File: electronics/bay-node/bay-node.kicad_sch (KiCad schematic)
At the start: 0 parts

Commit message: DATA lead on 8 wires: node J7 a vertical PH 8 (USB, I²C, INT), data port J2 an S8B
Density decisions of 2026-10-19: the DATA lead becomes the camera's PH 8
"Same direction" type and also carries the node's I²C and an open-drain,
active-low INT (IO4, 10k pull-up, 1k at J7) for a later DATA ×4 board.

- Node: J7 B8B vertical by the right edge (J5's old slot), J5 AUX
  horizontal in the middle, AUX parts in a column between them.  J7 now
  taps the pair at J4's pads (DUT_CONN_*, behind U8's ESD like J4); the
  branch is hand-drawn in usb_hs_routes() on B.Cu under J4, since
  Freerouting found no room on U8's mux side.  ERC 0, DRC 0, parity 0,
  99 models.
- Data port: S8B, pins 1–3 open, PH at x 14.4, left hole (2.6, 13.5),
  one silkscreen label per pin.  ERC 0, DRC 0, parity 0.
- Pin map (README, check_pinmap: DATA_INT reserved), docs, cabling,
  BOM (one PH 8 lead type for DATA and camera, no B5B/S5B), SCAD config.

Co-Authored-By: Claude Opus 5.5 <noreply@anthropic.com>
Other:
- note added: "DATA_INT, ESP_DN/DP, I2C_SCL/SDA,"
- note added: "DUT_5V, I2C_SCL/SDA"
- note added: "MUX_FORCE_PC, PC_DET, SVC"
- note removed: "DUT_5V"
- note removed: "ESP_DN/DP, MUX_FORCE_PC, PC_DET, SVC"
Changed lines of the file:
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@@
 		(pts
 			(xy 91.44 100.33)
-			(xy 91.44 110.49)
-			(xy 138.43 110.49)
+			(xy 91.44 113.03)
+			(xy 138.43 113.03)
 			(xy 138.43 100.33)
 		)
@@
 		)
 	)
-	(text "ESP_DN/DP, MUX_FORCE_PC, PC_DET, SVC"
+	(text "DATA_INT, ESP_DN/DP, I2C_SCL/SDA,"
 		(exclude_from_sim no)
 		(at 93.98 109.22 0)
+		(effects
+			(font
+				(size 1.4 1.4)
+			)
+			(justify left bottom)
+		)
+	)
+	(text "MUX_FORCE_PC, PC_DET, SVC"
+		(exclude_from_sim no)
+		(at 93.98 111.76 0)
 		(effects
 			(font
@@
 		(pts
 			(xy 179.07 100.33)
-			(xy 179.07 120.65)
-			(xy 232.41 120.65)
+			(xy 179.07 123.19)
+			(xy 232.41 123.19)
 			(xy 232.41 100.33)
 		)
@@
 		)
 	)
-	(text "DUT_5V"
+	(text "DUT_5V, I2C_SCL/SDA"
 		(exclude_from_sim no)
-		(at 181.61 119.38 0)
+		(at 181.61 121.92 0)
 		(effects
 			(font
@@
 		(pts
 			(xy 83.82 100.33)
-			(xy 83.82 130.81)
-			(xy 240.03 130.81)
+			(xy 83.82 133.35)
+			(xy 240.03 133.35)
 			(xy 240.03 100.33)
 		)
@@
 	(text "AUX_BOOT_CTL, AUX_RST_CTL, AUX_RX/TX, DUT_EN, DUT_FLT_N, I2C_SCL/SDA, INA_ALERT_N"
 		(exclude_from_sim no)
-		(at 86.36 129.54 0)
+		(at 86.36 132.08 0)
 		(effects
 			(font
@@
 		(pts
 			(xy 76.2 100.33)
-			(xy 76.2 140.97)
-			(xy 327.66 140.97)
+			(xy 76.2 143.51)
+			(xy 327.66 143.51)
 			(xy 327.66 100.33)
 		)
@@
 	(text "CAN_RXD/TXD, POS_IN/OUT"
 		(exclude_from_sim no)
-		(at 78.74 139.7 0)
+		(at 78.74 142.24 0)
 		(effects
 			(font
@@
 		(pts
 			(xy -2.54 100.33)
-			(xy -2.54 151.13)
-			(xy 335.28 151.13)
+			(xy -2.54 153.67)
+			(xy 335.28 153.67)
 			(xy 335.28 100.33)
 		)
@@
 	(text "CAN_H/L, POS_IN_CONN, POS_OUT_CONN"
 		(exclude_from_sim no)
-		(at 0 149.86 0)
+		(at 0 152.4 0)
 		(effects
 			(font
@@
 		(pts
 			(xy 68.58 100.33)
-			(xy 68.58 161.29)
-			(xy 421.64 161.29)
+			(xy 68.58 163.83)
+			(xy 421.64 163.83)
 			(xy 421.64 100.33)
 		)
@@
 	(text "CAM_CS/LED/SCK, CAM_MISO, CAM_MOSI"
 		(exclude_from_sim no)
-		(at 71.12 160.02 0)
+		(at 71.12 162.56 0)
 		(effects
 			(font
@@
 	(text_box "Bay node — one per bay.  Sheets:\n  Power: row cable (JST PH 6: bus, GND, CAN_H, CAN_L, GND, POS), reverse protection, LMR51635 buck, AMS1117\n  MCU: ESP32-S3-WROOM-1-N8R8 (8 MB flash, 8 MB octal PSRAM), reset/boot, status LED, UART pads\n  USB: front PC port, DUT port, two FSUSB42 muxes + OR gate (classic / USB-IP / service modes)\n  DUT power & AUX: TPS2553 switch → shunt → DUT_5V, INA226 monitor, AUX UART/RESET/BOOT\n  Camera: JST PH 8 to the bay's Arducam Mega (SPI2, 5 V through a PTC) and its LEDs (AO3400A low side)\n  Rack bus: TCAN1462V CAN transceiver on the row pair, POS token in/out (docs/can.md)\n\nMode truth table:  SERVICE=0, PC unplugged → DUT↔ESP32 (USB/IP)\n                   SERVICE=0, PC plugged   → DUT↔PC (classic), ESP32 still controls DUT_5V/AUX\n                   SERVICE=1               → PC↔ESP32 (flash/console), DUT data disconnected\nGPIO firmware can also force classic mode (MUX_FORCE_PC)."
 		(exclude_from_sim no)
-		(at 30 176.53 0)
+		(at 30 179.07 0)
 		(size 360 33.02)
 		(margins 2 2 2 2)

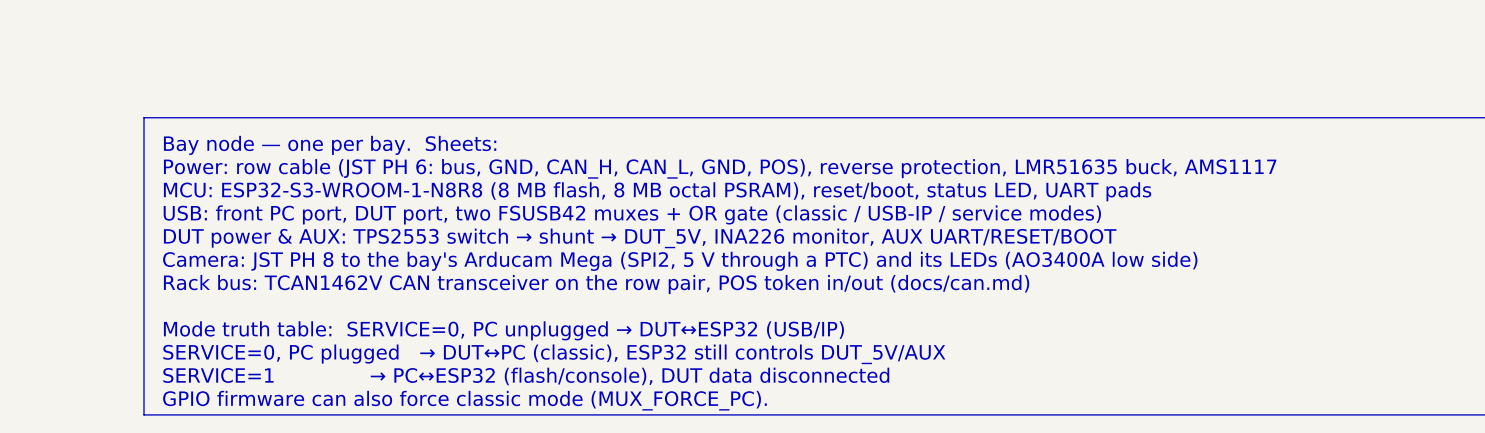
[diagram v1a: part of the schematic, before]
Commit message: CAN transceiver: the TJA1462AT on the hub and the node
The TCAN1462V (C7399456) had no LCSC stock on 2026-10-18 and 19, and
JLC's quote of the hub asked for another part.  The user chose NXP's
TJA1462AT/0Z (C3234095, 10 500 in stock) for both boards (hub U6, node
U11): the same SOIC-8 pinout (VIO on pin 5, STB on pin 8), signal
improvement kept, bus pins -36/+40 V instead of ±58 V.  The TCAN1462V
and the TCAN1044AV stay the alternates.

Both boards regenerated and the same Freerouting sessions re-imported
(tracks and vias unchanged): ERC 0, DRC 0 errors (the hub's known C8
silkscreen warning), 0 unconnected, parity 0, JLC READY.  The CPL keeps
its 270° correction (C3234095 was already in build_board.py).

Docs: can.md, electronics.md, firmware comments and pin tables,
bom/sourcing.md, which also notes that JLC unticks the USB4105 (hard to
process, $0.03 a piece): tick it again at every order.

Co-Authored-By: Claude Opus 5.5 <noreply@anthropic.com>
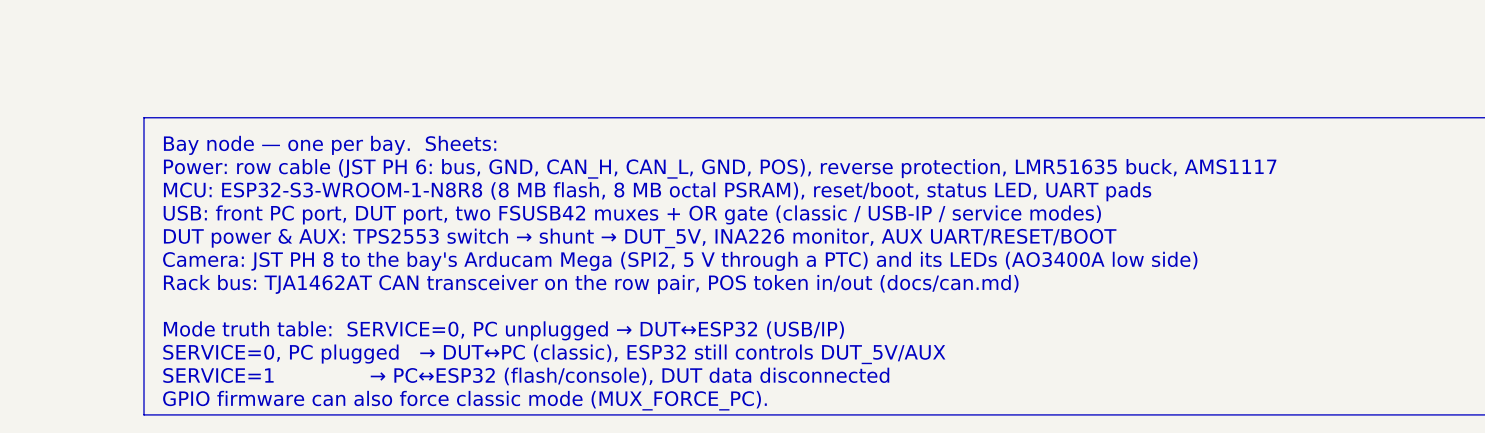
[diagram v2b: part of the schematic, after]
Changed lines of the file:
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@@
 		)
 	)
-	(text_box "Bay node — one per bay.  Sheets:\n  Power: row cable (JST PH 6: bus, GND, CAN_H, CAN_L, GND, POS), reverse protection, LMR51635 buck, AMS1117\n  MCU: ESP32-S3-WROOM-1-N8R8 (8 MB flash, 8 MB octal PSRAM), reset/boot, status LED, UART pads\n  USB: front PC port, DUT port, two FSUSB42 muxes + OR gate (classic / USB-IP / service modes)\n  DUT power & AUX: TPS2553 switch → shunt → DUT_5V, INA226 monitor, AUX UART/RESET/BOOT\n  Camera: JST PH 8 to the bay's Arducam Mega (SPI2, 5 V through a PTC) and its LEDs (AO3400A low side)\n  Rack bus: TCAN1462V CAN transceiver on the row pair, POS token in/out (docs/can.md)\n\nMode truth table:  SERVICE=0, PC unplugged → DUT↔ESP32 (USB/IP)\n                   SERVICE=0, PC plugged   → DUT↔PC (classic), ESP32 still controls DUT_5V/AUX\n                   SERVICE=1               → PC↔ESP32 (flash/console), DUT data disconnected\nGPIO firmware can also force classic mode (MUX_FORCE_PC)."
+	(text_box "Bay node — one per bay.  Sheets:\n  Power: row cable (JST PH 6: bus, GND, CAN_H, CAN_L, GND, POS), reverse protection, LMR51635 buck, AMS1117\n  MCU: ESP32-S3-WROOM-1-N8R8 (8 MB flash, 8 MB octal PSRAM), reset/boot, status LED, UART pads\n  USB: front PC port, DUT port, two FSUSB42 muxes + OR gate (classic / USB-IP / service modes)\n  DUT power & AUX: TPS2553 switch → shunt → DUT_5V, INA226 monitor, AUX UART/RESET/BOOT\n  Camera: JST PH 8 to the bay's Arducam Mega (SPI2, 5 V through a PTC) and its LEDs (AO3400A low side)\n  Rack bus: TJA1462AT CAN transceiver on the row pair, POS token in/out (docs/can.md)\n\nMode truth table:  SERVICE=0, PC unplugged → DUT↔ESP32 (USB/IP)\n                   SERVICE=0, PC plugged   → DUT↔PC (classic), ESP32 still controls DUT_5V/AUX\n                   SERVICE=1               → PC↔ESP32 (flash/console), DUT data disconnected\nGPIO firmware can also force classic mode (MUX_FORCE_PC)."
 		(exclude_from_sim no)
 		(at 30 179.07 0)

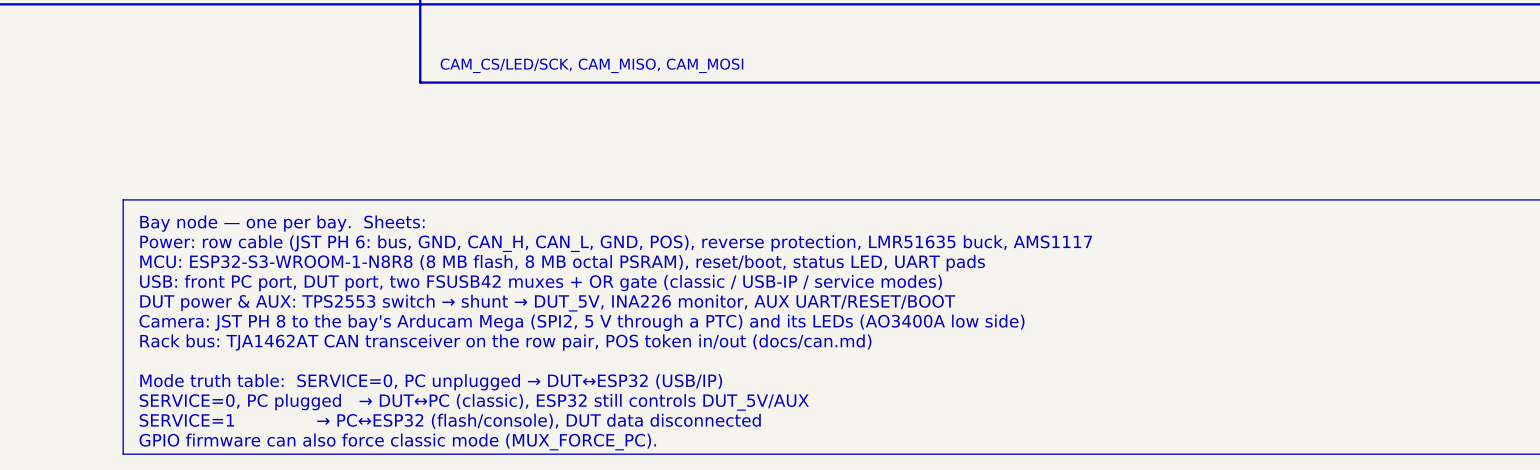
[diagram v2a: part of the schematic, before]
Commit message: Node 5 V buck: LMR51625 with TI's 4.7 µH
The bay node's U1 goes from the LMR51635YDDCR (3.5 A) to its 2.5 A
sibling, the LMR51625YDDCR (C44991044), as the user asked.  TI SLUSF64B
covers both parts: they have the same DDC package and pinout (FB 1,
EN 2, VIN 3, GND 4, SW 5, CB 6), the same 0.8 V reference, the same EN
thresholds and the same 63 V absolute maximum.

L1 goes to 4.7 µH, per SLUSF64B table 8-1 (LMR51625, 5 V, 1.1 MHz).
The new part is the FXL0630-4R7-M (C167220), in the same footprint:
9 A saturation, 6 A rms, 33 mΩ.  The existing 3 × 22 µF output meets
the table's 22 µF.

Current headroom: a bay draws at most 2.2 A (node 0.30 A, the DUT
switch's 1.52 A, camera 0.36 A).  From 28 V the inductor then peaks at
about 2.6 A (0.8 A ripple), under the 2.5 A part's 2.9 A minimum peak
limit.  With 3.3 µH the peak would be 2.74 A.

The hub keeps the LMR51635 under the "buck" catalogue key.  The node
uses two new keys, "buck25" and "buck_l47".

CPL: JLC's EasyEDA footprint of C44991044 is pad for pad that of
C45262770 and C7519, so it gets the same 270° correction.  C167220
shares C167219's footprint and needs no correction.

Board: schematic regenerated; the routed PCB keeps its routing (only
U1 and L1 properties change, copied from a fresh build).  ERC 0,
DRC 0, unconnected 0, parity 0.  Gerbers, CPL and renders unchanged.

Cost:
- node order $322.96 -> $316.95 (-$6.01 components: LCSC $1.0744
  against $1.5997 at 10, the inductor $0.096 against $0.107, × 1.12);
- one rack's JLC boards $752.95 -> $746.43 (5 racks $310.59,
  10 racks $257.85);
- BOM total €1,013 -> €1,007 (€126 a bay);
- the 9-instead-of-10 lever is now $2.34.

The parts snapshot gains the two parts.  The BOM note prints a
negative adjustment as "− $6.01", not "+ $-6.01".

Co-Authored-By: Claude Opus 5.5 <noreply@anthropic.com>
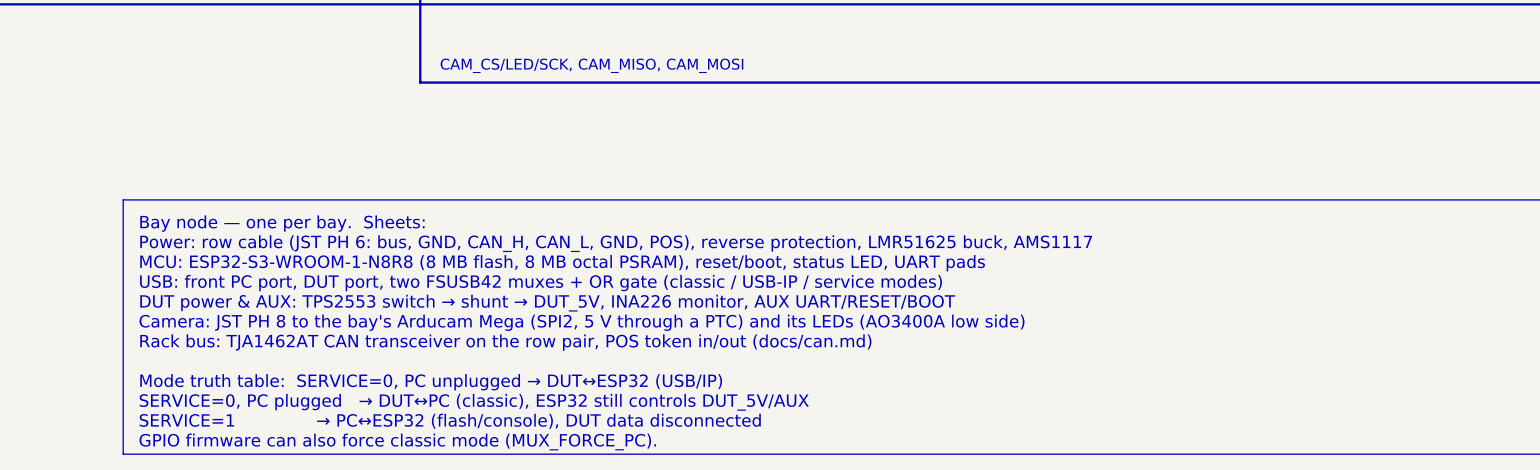
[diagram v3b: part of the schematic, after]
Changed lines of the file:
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@@
 		)
 	)
-	(text_box "Bay node — one per bay.  Sheets:\n  Power: row cable (JST PH 6: bus, GND, CAN_H, CAN_L, GND, POS), reverse protection, LMR51635 buck, AMS1117\n  MCU: ESP32-S3-WROOM-1-N8R8 (8 MB flash, 8 MB octal PSRAM), reset/boot, status LED, UART pads\n  USB: front PC port, DUT port, two FSUSB42 muxes + OR gate (classic / USB-IP / service modes)\n  DUT power & AUX: TPS2553 switch → shunt → DUT_5V, INA226 monitor, AUX UART/RESET/BOOT\n  Camera: JST PH 8 to the bay's Arducam Mega (SPI2, 5 V through a PTC) and its LEDs (AO3400A low side)\n  Rack bus: TJA1462AT CAN transceiver on the row pair, POS token in/out (docs/can.md)\n\nMode truth table:  SERVICE=0, PC unplugged → DUT↔ESP32 (USB/IP)\n                   SERVICE=0, PC plugged   → DUT↔PC (classic), ESP32 still controls DUT_5V/AUX\n                   SERVICE=1               → PC↔ESP32 (flash/console), DUT data disconnected\nGPIO firmware can also force classic mode (MUX_FORCE_PC)."
+	(text_box "Bay node — one per bay.  Sheets:\n  Power: row cable (JST PH 6: bus, GND, CAN_H, CAN_L, GND, POS), reverse protection, LMR51625 buck, AMS1117\n  MCU: ESP32-S3-WROOM-1-N8R8 (8 MB flash, 8 MB octal PSRAM), reset/boot, status LED, UART pads\n  USB: front PC port, DUT port, two FSUSB42 muxes + OR gate (classic / USB-IP / service modes)\n  DUT power & AUX: TPS2553 switch → shunt → DUT_5V, INA226 monitor, AUX UART/RESET/BOOT\n  Camera: JST PH 8 to the bay's Arducam Mega (SPI2, 5 V through a PTC) and its LEDs (AO3400A low side)\n  Rack bus: TJA1462AT CAN transceiver on the row pair, POS token in/out (docs/can.md)\n\nMode truth table:  SERVICE=0, PC unplugged → DUT↔ESP32 (USB/IP)\n                   SERVICE=0, PC plugged   → DUT↔PC (classic), ESP32 still controls DUT_5V/AUX\n                   SERVICE=1               → PC↔ESP32 (flash/console), DUT data disconnected\nGPIO firmware can also force classic mode (MUX_FORCE_PC)."
 		(exclude_from_sim no)
 		(at 30 179.07 0)

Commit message: Bay node: AP2114H for the 3.3 V, camera ESD clamped to +3V3
The schematic counter-review's fixes, approved by the user.

- U2: AP2114H-3.3TRG1 (C150716, catalog ldo_1a) instead of the AMS1117-3.3.
  It is specified stable with ceramics (C11, C12); the AMS1117 guarantees it
  only with 22 uF tantalum.  Same SOT-223 "H" pinout (1 GND, 2 and tab VOUT,
  3 VIN), footprint and copper: only the part's properties change.
- U12, U13 (USBLC6 on the camera lead): pin 5 on +3V3 instead of CAM_5V.
  With CAM_5V off (the PTC tripped), the SPI lines would feed the pod through
  the upper diodes, and CAM_5V's clamp sits above the ESP32's 3.6 V.  A
  minimal patch of the routing, no re-route: the CAM_5V stub that only
  reached the two pins goes (10 segments); U12.5 gets a +3V3 feed to a via in
  In2's +3V3 area; U13.5, with no room for its own, joins U12.5 along the
  stub's old east path at 0.25 mm.  The straightening pass ran on +3V3 and
  CAM_5V.
- Stale notes: AUX_VREF goes through R23's 1k, not 33 ohms; the next node's
  pull-down is R29's 470k, not 100k.
- pcbgen.fanout_pads takes `only` (REF.PAD), to fan out a few pads of a
  routed board.

ERC 0, DRC 0, unconnected 0, parity 0, every 3D model found.  The renders,
Gerbers and viewer model are regenerated (the unchanged iso render kept).
The schematic, the BOM and the docs (the node table, the CPL fix table, the
bring-up check, PCBA review N9) follow.  The hub and bom/ are untouched.

Co-Authored-By: Claude Opus 5.5 <noreply@anthropic.com>
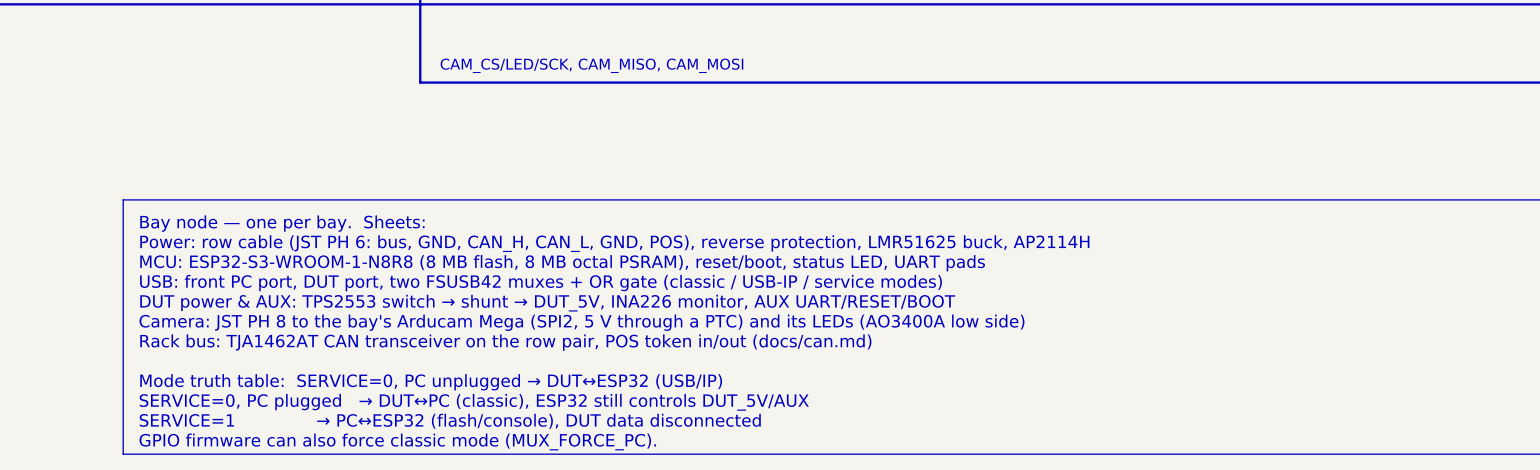
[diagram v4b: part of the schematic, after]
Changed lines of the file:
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@@
 		)
 	)
-	(text_box "Bay node — one per bay.  Sheets:\n  Power: row cable (JST PH 6: bus, GND, CAN_H, CAN_L, GND, POS), reverse protection, LMR51625 buck, AMS1117\n  MCU: ESP32-S3-WROOM-1-N8R8 (8 MB flash, 8 MB octal PSRAM), reset/boot, status LED, UART pads\n  USB: front PC port, DUT port, two FSUSB42 muxes + OR gate (classic / USB-IP / service modes)\n  DUT power & AUX: TPS2553 switch → shunt → DUT_5V, INA226 monitor, AUX UART/RESET/BOOT\n  Camera: JST PH 8 to the bay's Arducam Mega (SPI2, 5 V through a PTC) and its LEDs (AO3400A low side)\n  Rack bus: TJA1462AT CAN transceiver on the row pair, POS token in/out (docs/can.md)\n\nMode truth table:  SERVICE=0, PC unplugged → DUT↔ESP32 (USB/IP)\n                   SERVICE=0, PC plugged   → DUT↔PC (classic), ESP32 still controls DUT_5V/AUX\n                   SERVICE=1               → PC↔ESP32 (flash/console), DUT data disconnected\nGPIO firmware can also force classic mode (MUX_FORCE_PC)."
+	(text_box "Bay node — one per bay.  Sheets:\n  Power: row cable (JST PH 6: bus, GND, CAN_H, CAN_L, GND, POS), reverse protection, LMR51625 buck, AP2114H\n  MCU: ESP32-S3-WROOM-1-N8R8 (8 MB flash, 8 MB octal PSRAM), reset/boot, status LED, UART pads\n  USB: front PC port, DUT port, two FSUSB42 muxes + OR gate (classic / USB-IP / service modes)\n  DUT power & AUX: TPS2553 switch → shunt → DUT_5V, INA226 monitor, AUX UART/RESET/BOOT\n  Camera: JST PH 8 to the bay's Arducam Mega (SPI2, 5 V through a PTC) and its LEDs (AO3400A low side)\n  Rack bus: TJA1462AT CAN transceiver on the row pair, POS token in/out (docs/can.md)\n\nMode truth table:  SERVICE=0, PC unplugged → DUT↔ESP32 (USB/IP)\n                   SERVICE=0, PC plugged   → DUT↔PC (classic), ESP32 still controls DUT_5V/AUX\n                   SERVICE=1               → PC↔ESP32 (flash/console), DUT data disconnected\nGPIO firmware can also force classic mode (MUX_FORCE_PC)."
 		(exclude_from_sim no)
 		(at 30 179.07 0)
